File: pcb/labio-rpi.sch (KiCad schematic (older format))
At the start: 12 parts, among them IC201 AT24CS32-XHM, P1 CONN_02X20, U201 AP7365_SOT-23-5

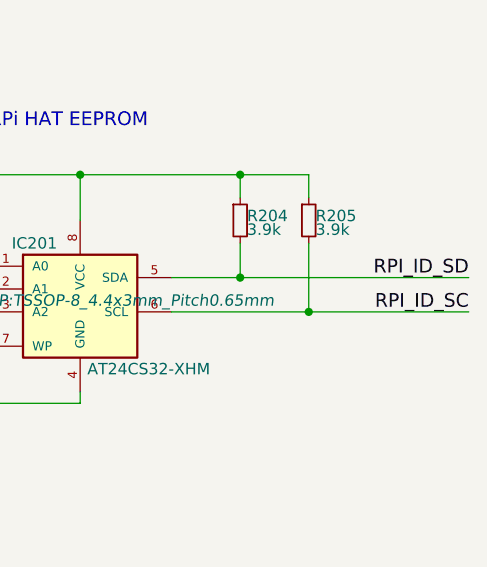
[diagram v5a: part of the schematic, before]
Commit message: floorplan on 150x85mm board, use al caps for motors
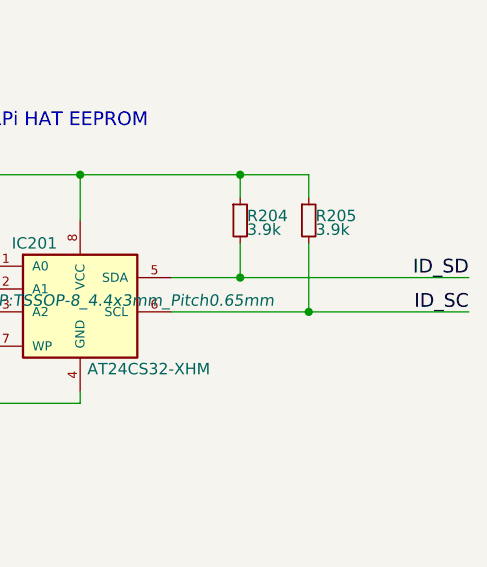
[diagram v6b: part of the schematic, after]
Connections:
- net RPI_ID_SC is gone; now on net ID_SC: IC201.6 (SCL), R205.2
- net RPI_ID_SD is gone; now on net ID_SD: IC201.5 (SDA), R204.2
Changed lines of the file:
@@
 Connection ~ 7400 2500
 Text Label 9900 1950 2    60   ~ 0
-RPI_ID_SD
+ID_SD
 Text Label 9900 2100 2    60   ~ 0
-RPI_ID_SC
+ID_SC
 Text HLabel 7300 1500 0    60   Input ~ 0
 3V3_2

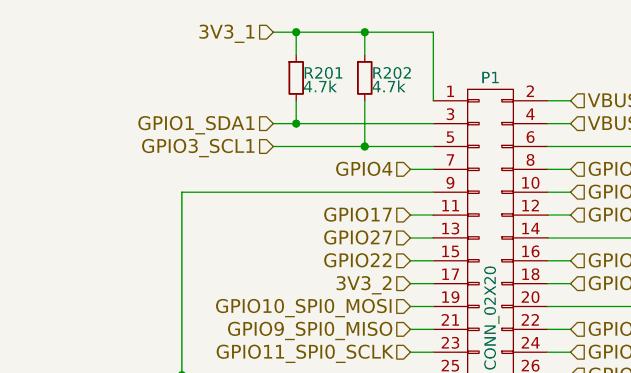
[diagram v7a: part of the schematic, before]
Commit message: shrink board to 85x150mm with tab board under rpi 0/debugger
* use space under rpi 0/debugger for imu since no visibility is needed
* rearrange dpad buttons and speaker to be more compact
* use 3V3_EXTRA for i2c pullups for consistency
* add bottom right hole to match future power module
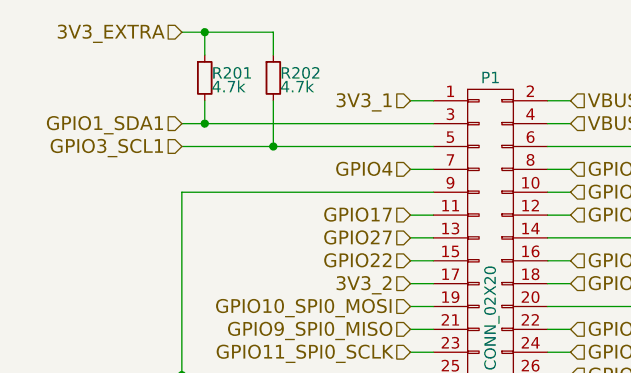
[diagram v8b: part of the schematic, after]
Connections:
- net 3V3_1: no longer R201.1, R202.1
- net 3V3_EXTRA: now also R201.1, R202.1
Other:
- moved on the sheet: R201, R202
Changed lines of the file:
@@
 	3900 1400 4000 1400
 Wire Wire Line
-	4000 1300 3300 1300
+	2900 1300 4000 1300
 Wire Wire Line
-	3300 1200 4000 1200
+	2900 1200 4000 1200
 Text Label 4900 2400 2    60   ~ 0
 ID_SC
-Text HLabel 3300 800  0    60   Input ~ 0
+Text HLabel 3900 1100 0    60   Input ~ 0
 3V3_1
-Text HLabel 3300 1200 0    60   Input ~ 0
+Text HLabel 2900 1200 0    60   Input ~ 0
 GPIO1_SDA1
-Text HLabel 3300 1300 0    60   Input ~ 0
+Text HLabel 2900 1300 0    60   Input ~ 0
 GPIO3_SCL1
 Text HLabel 3900 1400 0    60   Input ~ 0
@@
 L R_Small R202
 U 1 1 5766CCA0
-P 3700 1000
-F 0 "R202" H 3730 1020 50  0000 L CNN
-F 1 "4.7k" H 3730 960 50  0000 L CNN
-F 2 "Resistors_SMD:R_0603" H 3700 1000 50  0001 C CNN
-F 3 "" H 3700 1000 50  0000 C CNN
-	1    3700 1000
+P 3300 1000
+F 0 "R202" H 3330 1020 50  0000 L CNN
+F 1 "4.7k" H 3330 960 50  0000 L CNN
+F 2 "Resistors_SMD:R_0603" H 3300 1000 50  0001 C CNN
+F 3 "" H 3300 1000 50  0000 C CNN
+	1    3300 1000
 	1    0    0    -1
 $EndComp
@@
 L R_Small R201
 U 1 1 5766CD8E
-P 3400 1000
-F 0 "R201" H 3430 1020 50  0000 L CNN
-F 1 "4.7k" H 3430 960 50  0000 L CNN
-F 2 "Resistors_SMD:R_0603" H 3400 1000 50  0001 C CNN
-F 3 "" H 3400 1000 50  0000 C CNN
-	1    3400 1000
+P 3000 1000
+F 0 "R201" H 3030 1020 50  0000 L CNN
+F 1 "4.7k" H 3030 960 50  0000 L CNN
+F 2 "Resistors_SMD:R_0603" H 3000 1000 50  0001 C CNN
+F 3 "" H 3000 1000 50  0000 C CNN
+	1    3000 1000
 	1    0    0    -1
 $EndComp
 Wire Wire Line
-	4000 1100 4000 800
+	3000 1100 3000 1200
+Connection ~ 3000 1200
 Wire Wire Line
-	4000 800  3300 800
-Wire Wire Line
-	3400 900  3400 800
-Connection ~ 3400 800
-Wire Wire Line
-	3400 1100 3400 1200
-Connection ~ 3400 1200
-Wire Wire Line
-	3700 900  3700 800
-Connection ~ 3700 800
-Wire Wire Line
-	3700 1100 3700 1300
-Connection ~ 3700 1300
+	3300 1100 3300 1300
+Connection ~ 3300 1300
 $Comp
 L AP7365_SOT-23-5 U201
@@
 Text HLabel 9200 4100 2    60   Input ~ 0
 3V3_EXTRA
+Wire Wire Line
+	3900 1100 4000 1100
+Text HLabel 2900 800  0    60   Input ~ 0
+3V3_EXTRA
+Wire Wire Line
+	2900 800  3300 800
+Wire Wire Line
+	3000 800  3000 900
+Wire Wire Line
+	3300 800  3300 900
+Connection ~ 3000 800
 $EndSCHEMATC
